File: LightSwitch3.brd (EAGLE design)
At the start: 22 x 62 mm, 4 parts, among them SW1 SWITCH-SPDT-ILLUMINATED, SW2 SWITCH-SPDT-ILLUMINATED, SW3 SWITCH-SPDT-ILLUMINATED

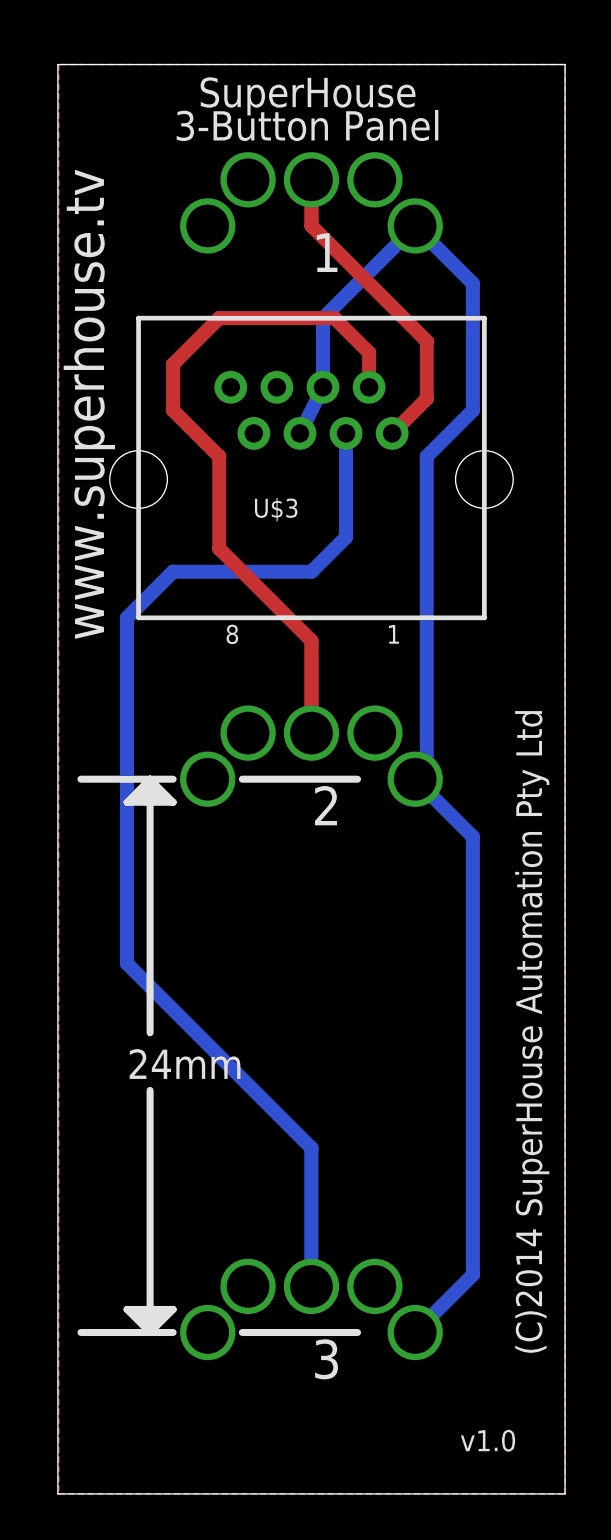
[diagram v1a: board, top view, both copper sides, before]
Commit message: Replaced buttons with more common SPST type
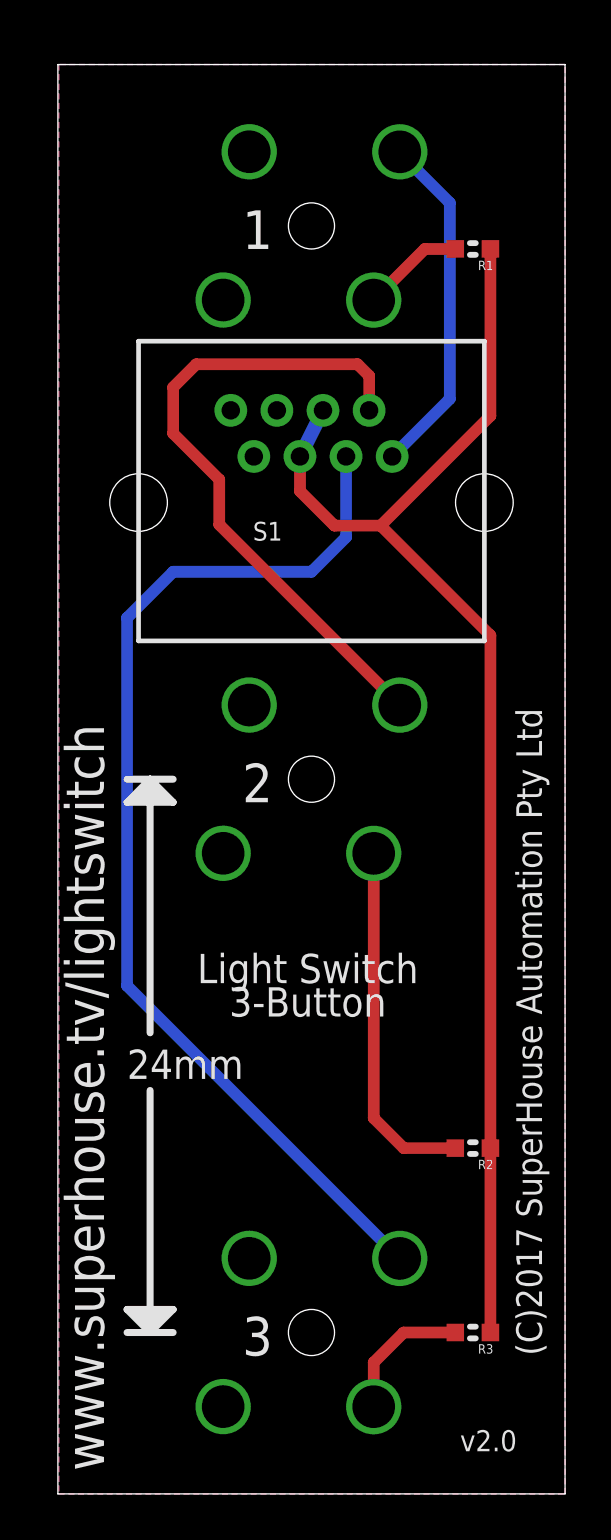
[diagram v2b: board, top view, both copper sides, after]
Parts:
- removed U$3: RJ45, freetronics-jon:RJ45
- added R1, R2, R3: 3K3, freetronics-jon:0603
- added S1: RJ45, freetronics-jon:RJ45
- SW1, SW2, SW3: value SWITCH-SPDT-ILLUMINATED -> SWITCH-SPST-ILLUMINATED; device freetronics-jon:SWITCH-SPDT-ILLUMINATED -> freetronics-jon:SWITCH-SPST-ILLUMINATED
- turned SW1 to 50 degrees
- turned SW2 to 50 degrees
- turned SW3 to 50 degrees
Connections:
- new net N$1: R1.2, SW1.2
- new net N$3: R2.2, SW2.2
- new net N$6: R3.2, SW3.2
- net +12V: now also R1.1, R2.1, R3.1, S1.4, S1.5; no longer SW1.1, SW2.1, SW3.1, U$3.4, U$3.5
- net GND: now also S1.7, S1.8, SW1.1, SW1.4, SW2.1, SW2.4, SW3.1, SW3.4; no longer SW1.2, SW1.5, SW2.2, SW2.5, SW3.2, SW3.5, U$3.7, U$3.8
- net N$2: now also S1.3, SW3.3; no longer SW3.4, U$3.3
- net N$4: now also S1.1, SW1.3; no longer SW1.4, U$3.1
- net N$5: now also S1.2, SW2.3; no longer SW2.4, U$3.2
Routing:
- net N$3: track 0.00 -> 15.6 mm
- net N$6: track 0.00 -> 5.99 mm
- net N$1: track 0.00 -> 4.46 mm
- net +12V: track 63.0 -> 58.8 mm
- net N$4: track 13.7 -> 15.1 mm
- net N$5: track 29.9 -> 28.5 mm
- net N$2: track 47.8 -> 47.1 mm
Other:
- board text added: "(C)2017 SuperHouse Automation Pty Ltd"
- board text added: "Light Switch 3-Button"
- board text added: "v2.0"
- board text added: "www.superhouse.tv/lightswitch"
- board text removed: "(C)2014 SuperHouse Automation Pty Ltd"
- board text removed: "8"
- board text removed: "SuperHouse 3-Button Panel"
- board text removed: "v1.0"
- board text removed: "www.superhouse.tv"
